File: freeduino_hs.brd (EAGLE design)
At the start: 68.6 x 53.3 mm, 46 parts, among them J1 DC-005, Q1 16 MHz, Q2 12 MHz, T1 FDN340P, U1 CH340G, U2 LM393D, U3 ATMEGA328P-PU, U4 REG1117, U5 REG1117, X1 MINI-USB-32005-201

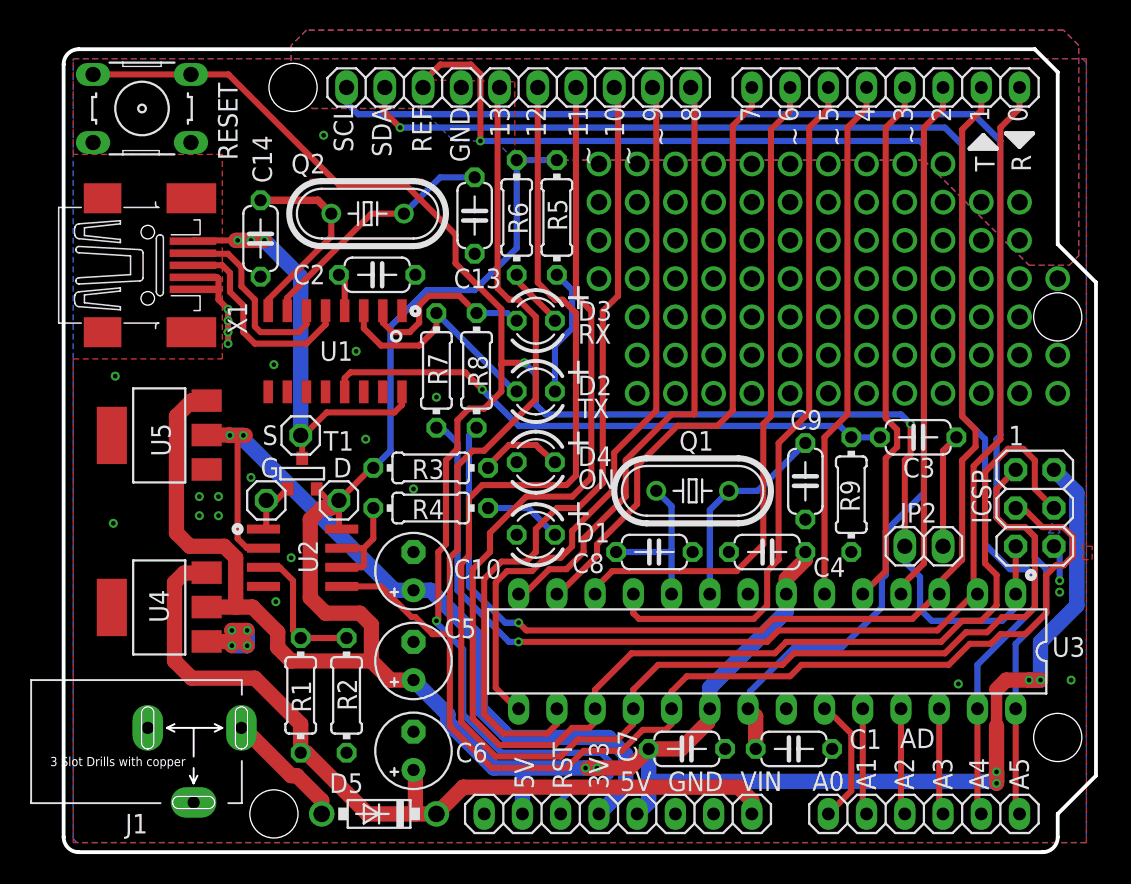
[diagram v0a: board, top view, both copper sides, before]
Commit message: Fix TX-RX routing
Move ISP connector
Add reset pull-up resistor
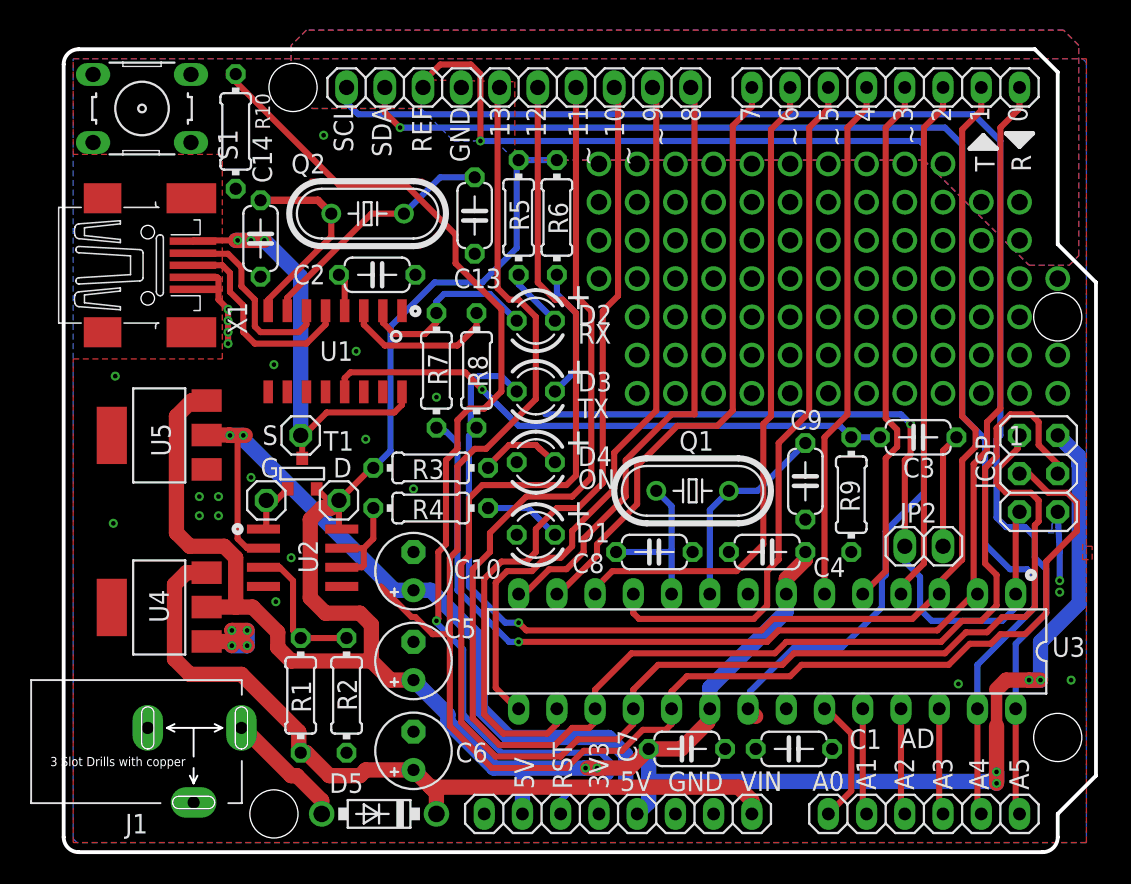
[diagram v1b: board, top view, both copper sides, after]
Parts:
- added R10: 10k, resistor:0204/7
- R5, R6: value 1k -> 6.8k
- R7, R8: value 1k -> 220
- S1: value TS42031-160R-TR-7260 -> RESET
- moved D2 4.70 mm to (31.4, 35.3)
- moved D3 4.70 mm to (31.4, 30.6)
- moved R6 2.67 mm to (32.8, 42.2)
- moved R5 2.54 mm to (30.2, 42.2)
- moved ICSP 2.30 mm to (64.8, 25.1)
- renumbered RESET to S1
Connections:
- net VIN renamed V+
- removed net M8TXD: D3.K, R8.1, U1.2
- new net N$93: D2.K, R7.1, U1.2
- net GND: now also R10.2
- net IO1: now also D3.K
- net M8RXD: now also R8.1; no longer D2.K, R7.1
- net RESET: now also R10.1
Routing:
- net N$93: track 0.00 -> 12.7 mm
- net M8TXD: track 12.3 -> 0.00 mm
- net RESET: track 135.7 -> 123.5 mm, vias 3 -> 2
- net IO1: track 79.8 -> 85.8 mm
- net M8RXD: track 15.5 -> 10.4 mm
- net N$36: track 8.64 -> 4.05 mm
- net N$35: track 4.62 -> 9.11 mm
- net MISO: track 106.3 -> 109.1 mm
- net V+: track 56.3 -> 53.5 mm
- net MOSI: track 105.3 -> 107.9 mm
- net +3V3: track 54.5 -> 52.0 mm
- net +5V: track 181.3 -> 183.6 mm
- net AREF: track 86.0 -> 83.8 mm
- net GND: track 19.7 -> 21.9 mm
- net SCK: track 112.3 -> 111.8 mm

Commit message: Re-route some traces
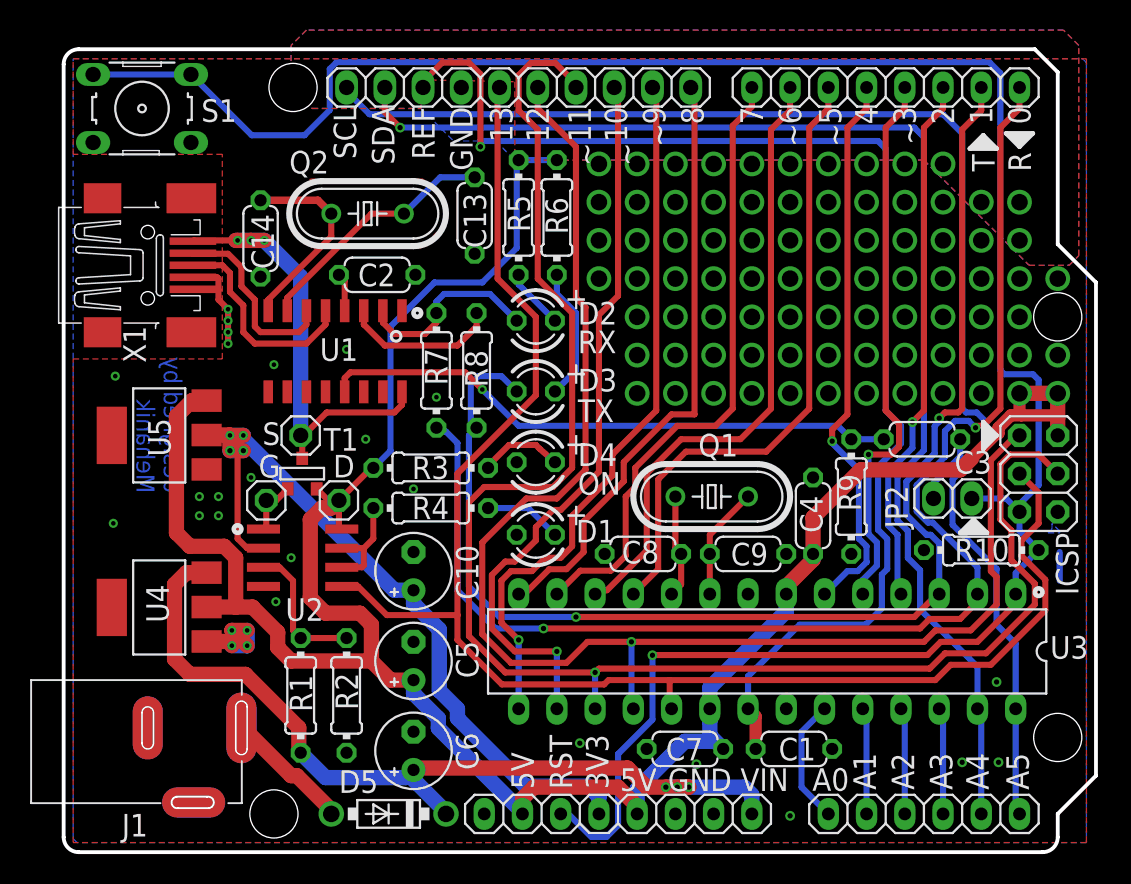
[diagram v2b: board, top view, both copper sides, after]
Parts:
- C1, C2, C3, C4, C7: device SmartPrj:C050-024X044 -> rcl_edited:C050-024X044
- C13, C14, C8, C9: device rcl:C050-024X044 -> rcl_edited:C050-024X044
- J1: device Seeed-OPL-Connector:DCJ3P-14.2X11.0X9.0MM -> OPL_Connector:DCJ3P-14.2X11.0X9.0MM
- U2: value LM393D -> LM358
- moved R10 56.8 mm to (61.0, 20.1), turned to 180 degrees
- moved C9 6.15 mm to (45.5, 19.8), turned to 180 degrees
- moved C4 3.89 mm to (49.8, 22.4), turned to 270 degrees
- moved JP2 3.70 mm to (59.1, 23.5), turned to 180 degrees
- moved Q1 1.33 mm to (43.1, 23.6)
- moved C8 0.77 mm to (38.5, 19.8), turned to 0 degrees
- moved D5 0.64 mm to (21.6, 2.54)
- moved C3 0.28 mm to (57.0, 27.4)
- moved C7 0.13 mm to (41.3, 6.86), turned to 0 degrees
- moved R9 0.13 mm to (52.3, 23.6)
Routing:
- net RESET: track 123.5 -> 151.4 mm, vias 2 -> 1
- net +5V: track 183.6 -> 161.0 mm, vias 6 -> 2
- net MISO: track 109.1 -> 95.1 mm, vias 0 -> 1
- net SCK: track 111.8 -> 103.6 mm
- net XTAL1: track 13.8 -> 7.53 mm
- net IO0: track 83.5 -> 88.8 mm, vias 1 -> 2
- net SS: track 53.9 -> 49.1 mm, vias 0 -> 1
- net IO5: track 46.8 -> 42.1 mm
- net V+: track 53.5 -> 57.7 mm, vias 0 -> 3
- net XTAL2: track 11.0 -> 6.90 mm
- net AD4/SDA: track 89.7 -> 86.1 mm
- net N$4: track 7.61 -> 4.67 mm
- net GND: track 21.9 -> 19.2 mm, vias 27 -> 30
- net IO1: track 85.8 -> 88.3 mm, vias 1 -> 2
- net IO4: track 34.8 -> 37.1 mm, vias 0 -> 1
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- removed copper zone on layer 1, net N$90
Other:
- board text added: "FREEDUINO"
- board text added: "HACKSPACE NSU"
- board text added: "Mehanik"
- board text added: "TH/NSU v1.0"
- board text added: "designed by"

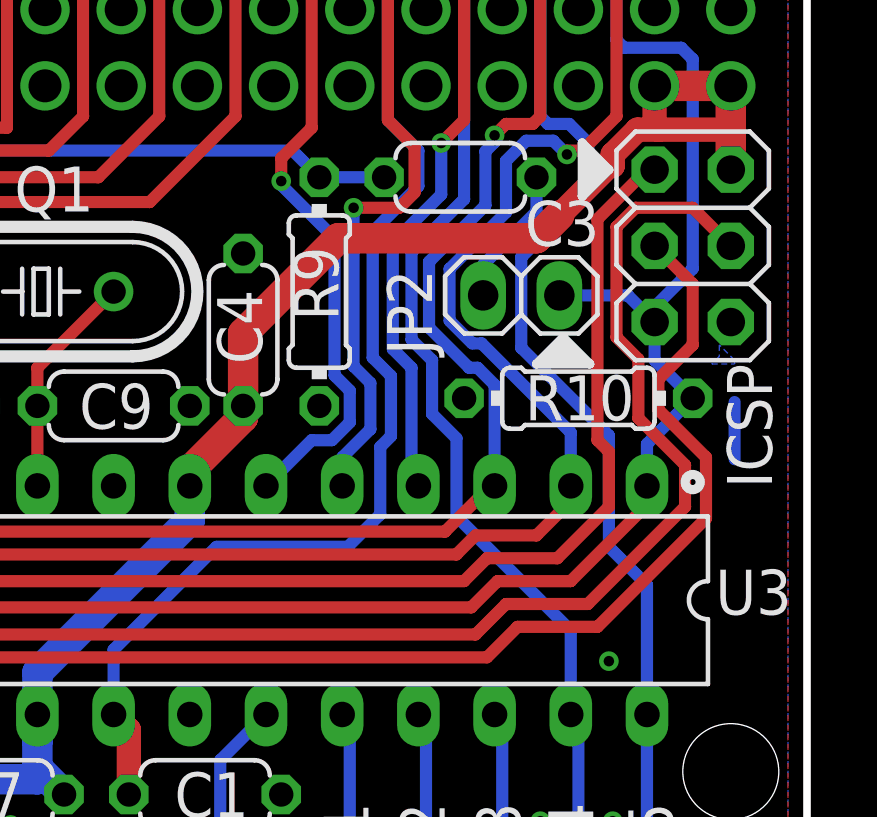
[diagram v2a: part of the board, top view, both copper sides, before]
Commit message: Fix reset pull-up
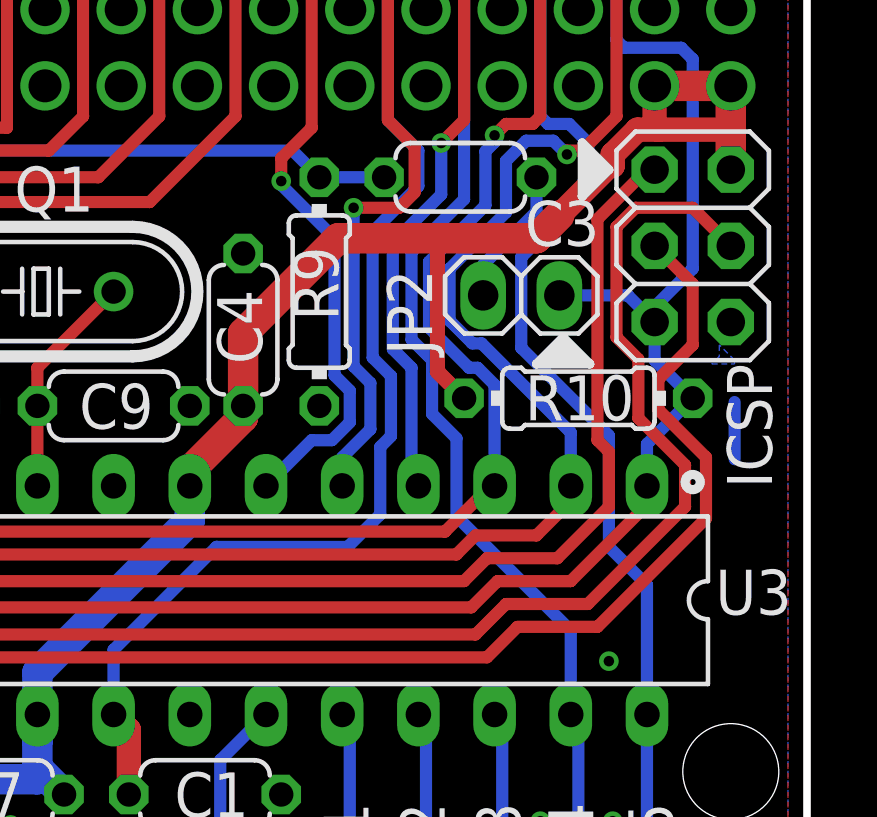
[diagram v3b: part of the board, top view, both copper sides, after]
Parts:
- U2: value LM358 -> LMV358
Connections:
- net +5V: now also R10.2
- net GND: no longer R10.2
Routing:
- net +5V: track 161.0 -> 166.7 mm
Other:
- board text added: "TH/NSU v1.1"
- board text removed: "TH/NSU v1.0"
